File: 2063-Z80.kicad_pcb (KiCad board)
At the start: 4 copper layers, 100 x 100 mm, 80 parts, among them J1 Conn_01x05, J10 Conn_01x07, J11 Conn_02x03_Odd_Even, J2 DM3D-SF(41), J3 Conn_02x20_Counter_Clockwise, J4 Conn_02x05_Odd_Even, J5 Conn_02x05_Odd_Even, J6 0548190519, J7 Conn_02x13_Top_Bottom, J8 Conn_01x05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

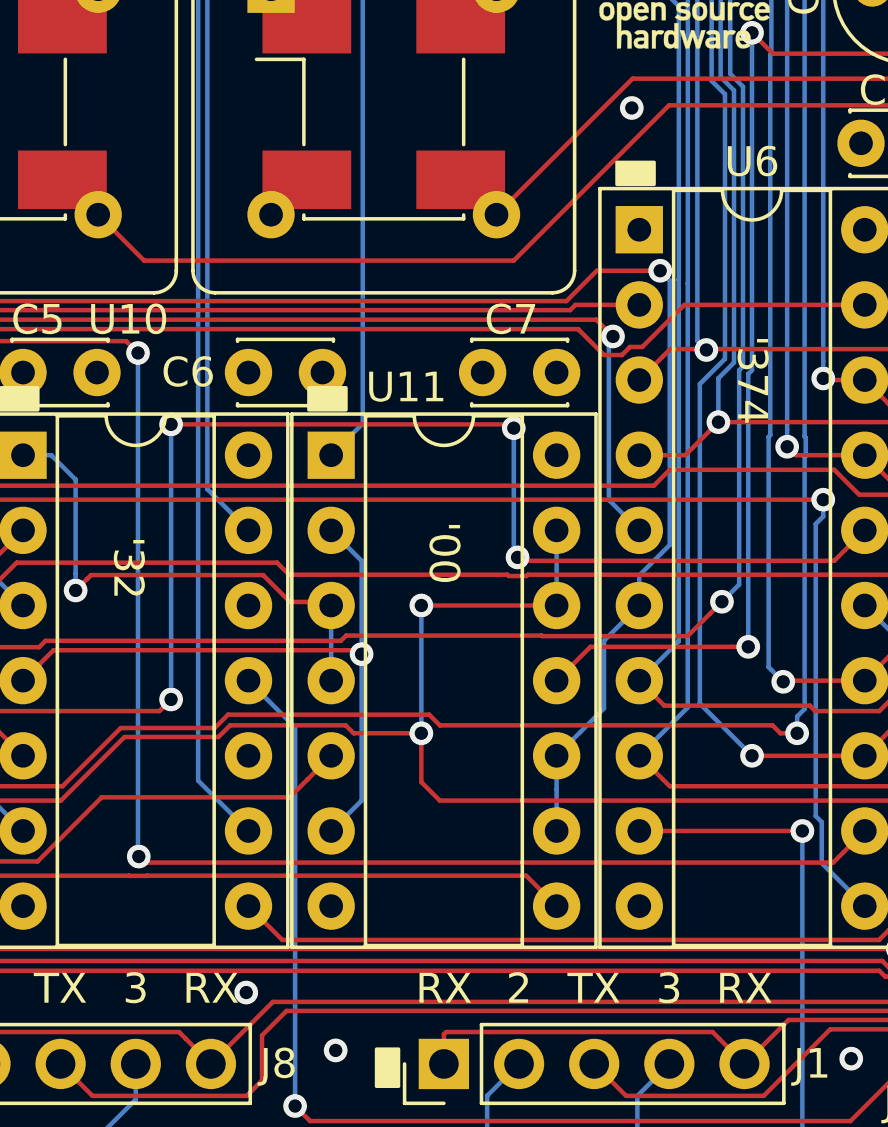
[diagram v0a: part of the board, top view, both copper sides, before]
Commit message: Change U11 symbol to a Schmitt NAND
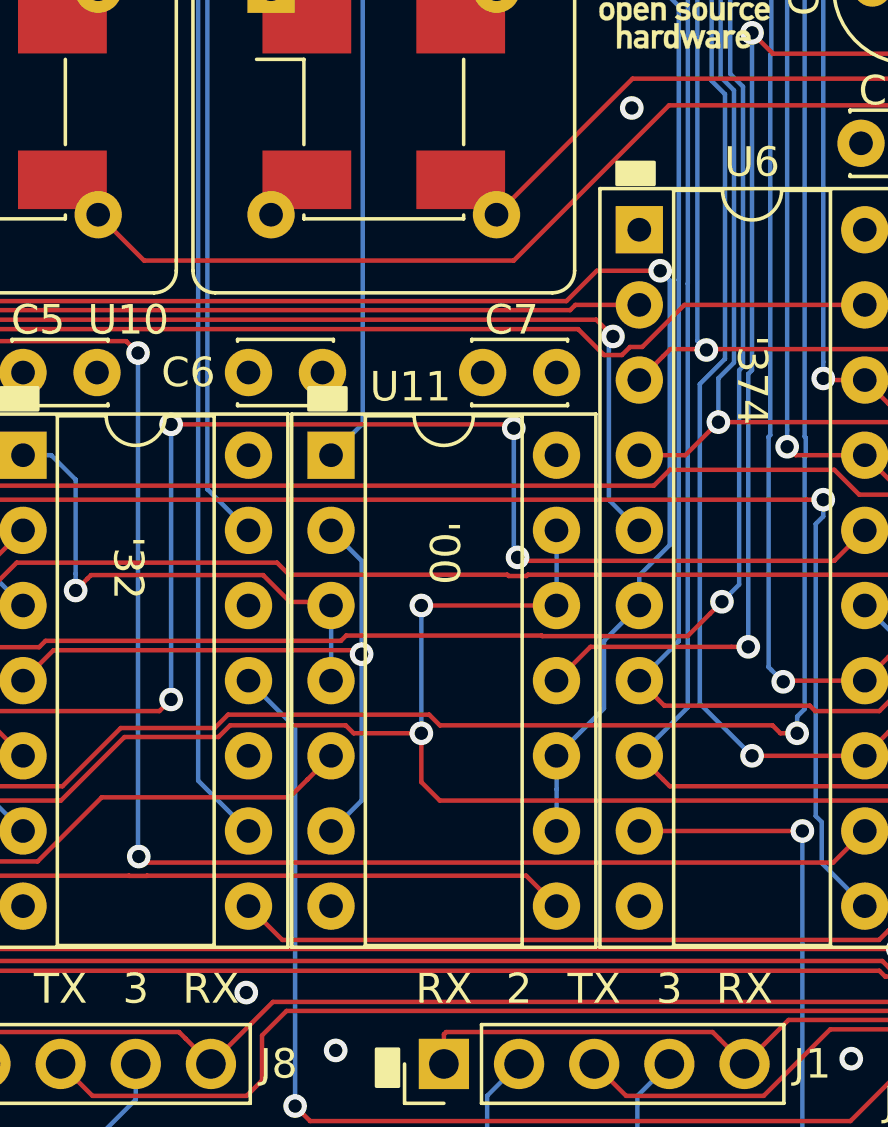
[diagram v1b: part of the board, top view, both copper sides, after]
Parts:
- U11: value 74HCT132E -> 74LS132
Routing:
- net /BAUD_CLK: track 65.6 -> 67.3 mm

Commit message: Revise BOM to reflect the as-built board.
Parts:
- U1: value Z80CPU -> Z80-CPU
- U10, U13: value 74LS32 -> 74HC32
- U11: value 74LS132 -> 74HCT132
- U4: value Z80_CTC -> Z80-CTC
- U6, U7: value 74LS374 -> 74HC374
- U9: value 74LS138 -> 74HC138
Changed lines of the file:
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@@
       (effects (font (size 1 1) (thickness 0.15)))
     )
-    (fp_text value 74LS132 (at 3.81 17.57) (layer F.Fab)
+    (fp_text value 74HCT132 (at 3.81 17.57) (layer F.Fab)
       (effects (font (size 1 1) (thickness 0.15)))
     )
@@
       (effects (font (size 1 1) (thickness 0.15)))
     )
-    (fp_text value 74LS32 (at 3.81 17.57) (layer F.Fab)
+    (fp_text value 74HC32 (at 3.81 17.57) (layer F.Fab)
       (effects (font (size 1 1) (thickness 0.15)))
     )
@@
       (effects (font (size 1 1) (thickness 0.15)))
     )
-    (fp_text value 74LS32 (at 3.81 17.57) (layer F.Fab)
+    (fp_text value 74HC32 (at 3.81 17.57) (layer F.Fab)
       (effects (font (size 1 1) (thickness 0.15)))
     )
@@
       (effects (font (size 1 1) (thickness 0.15)))
     )
-    (fp_text value Z80CPU (at 7.8994 45.5676) (layer F.Fab)
+    (fp_text value Z80-CPU (at 7.8994 45.5676) (layer F.Fab)
       (effects (font (size 1 1) (thickness 0.15)))
     )
@@
       (effects (font (size 1 1) (thickness 0.15)))
     )
-    (fp_text value Z80_CTC (at 7.62 35.35) (layer F.Fab)
+    (fp_text value Z80-CTC (at 7.62 35.35) (layer F.Fab)
       (effects (font (size 1 1) (thickness 0.15)))
     )
@@
       (effects (font (size 1 1) (thickness 0.15)))
     )
-    (fp_text value 74LS374 (at 3.81 25.19) (layer F.Fab)
+    (fp_text value 74HC374 (at 3.81 25.19) (layer F.Fab)
       (effects (font (size 1 1) (thickness 0.15)))
     )
@@
       (effects (font (size 1 1) (thickness 0.15)))
     )
-    (fp_text value 74LS374 (at 3.81 25.19) (layer F.Fab)
+    (fp_text value 74HC374 (at 3.81 25.19) (layer F.Fab)
       (effects (font (size 1 1) (thickness 0.15)))
     )
@@
       (effects (font (size 1 1) (thickness 0.15)))
     )
-    (fp_text value 74LS138 (at 3.81 20.11) (layer F.Fab)
+    (fp_text value 74HC138 (at 3.81 20.11) (layer F.Fab)
       (effects (font (size 1 1) (thickness 0.15)))
     )

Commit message: Clean up BOM values & formatting
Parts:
- J11: value Conn_02x03_Odd_Even -> Conn_02x03
- J3: value Conn_02x20_Counter_Clockwise -> Conn_02x20
- J4, J5: value Conn_02x05_Odd_Even -> Conn_02x05
- J7: value Conn_02x13_Top_Bottom -> Conn_02x13
- LOGO1, LOGO2: value Logo_Open_Hardware_Small -> OSHW_Logo
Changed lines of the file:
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@@
       (effects (font (size 1 1) (thickness 0.15)))
     )
-    (fp_text value Conn_02x03_Odd_Even (at 1.27 7.41 90) (layer F.Fab)
+    (fp_text value Conn_02x03 (at 1.27 7.41 90) (layer F.Fab)
       (effects (font (size 1 1) (thickness 0.15)))
     )
@@
       (effects (font (size 1 1) (thickness 0.15)))
     )
-    (fp_text value Conn_02x05_Odd_Even (at 1.27 12.49 90) (layer F.Fab)
+    (fp_text value Conn_02x05 (at 1.27 12.49 90) (layer F.Fab)
       (effects (font (size 1 1) (thickness 0.15)))
     )
@@
       (effects (font (size 1 1) (thickness 0.15)))
     )
-    (fp_text value Conn_02x05_Odd_Even (at 1.27 12.49 90) (layer F.Fab)
+    (fp_text value Conn_02x05 (at 1.27 12.49 90) (layer F.Fab)
       (effects (font (size 1 1) (thickness 0.15)))
     )
@@
       (effects (font (size 1 1) (thickness 0.15)))
     )
-    (fp_text value Logo_Open_Hardware_Small (at 0.75 0) (layer F.Fab) hide
+    (fp_text value OSHW_Logo (at 0.75 0) (layer F.Fab) hide
       (effects (font (size 1 1) (thickness 0.15)))
     )
@@
       (effects (font (size 1 1) (thickness 0.15)) (justify mirror))
     )
-    (fp_text value Logo_Open_Hardware_Small (at 0.75 0 90) (layer B.Fab) hide
+    (fp_text value OSHW_Logo (at 0.75 0 90) (layer B.Fab) hide
       (effects (font (size 1 1) (thickness 0.15)) (justify mirror))
     )
@@
       (effects (font (size 1 1) (thickness 0.15)))
     )
-    (fp_text value Conn_02x13_Top_Bottom (at 1.27 32.81 90) (layer F.Fab)
+    (fp_text value Conn_02x13 (at 1.27 32.81 90) (layer F.Fab)
       (effects (font (size 1 1) (thickness 0.15)))
     )
@@
       (effects (font (size 1 1) (thickness 0.15)))
     )
-    (fp_text value Conn_02x20_Counter_Clockwise (at 1.143 31.877 90) (layer F.Fab)
-      (effects (font (size 1 1) (thickness 0.15)))
-    )
+    (fp_text value Conn_02x20 (at 1.143 31.877 90) (layer F.Fab)
+      (effects (font (size 1 1) (thickness 0.15)))
+    )

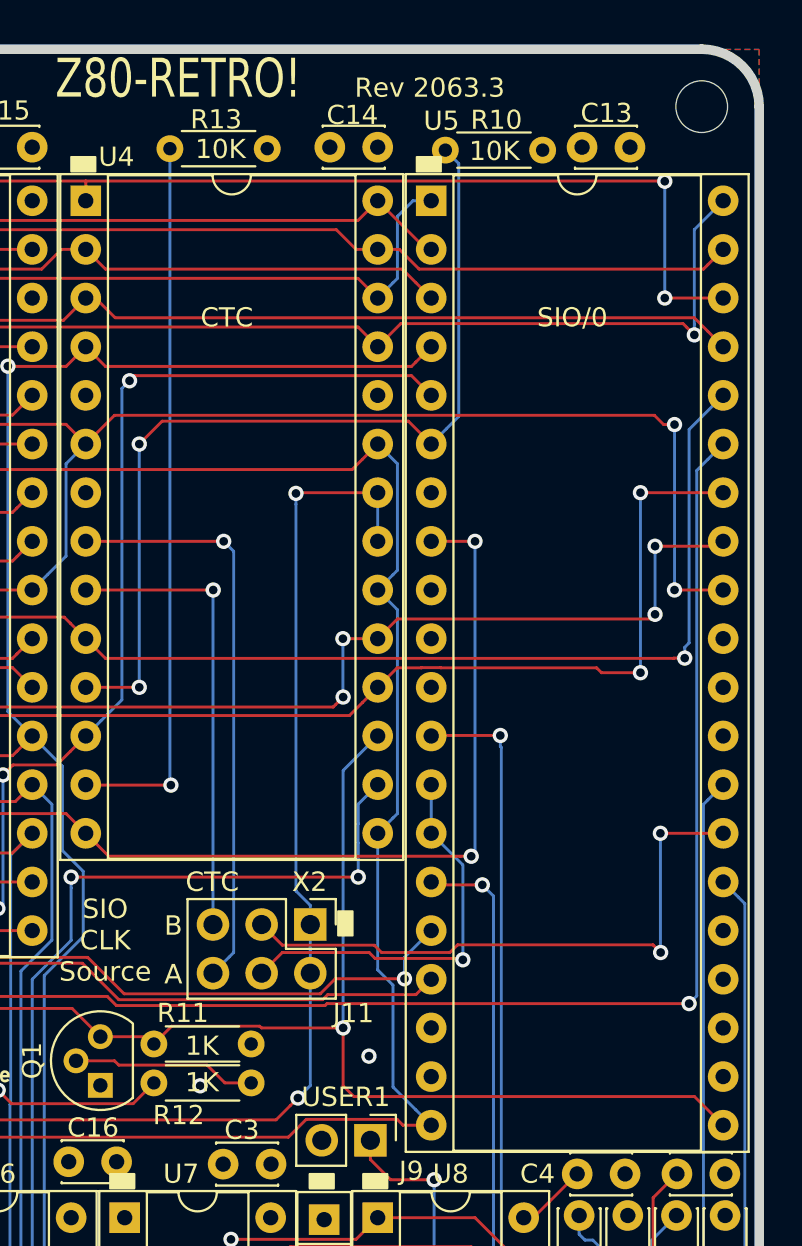
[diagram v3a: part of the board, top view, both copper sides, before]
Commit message: Move ~PRN_LF from U5.17 to U5.25
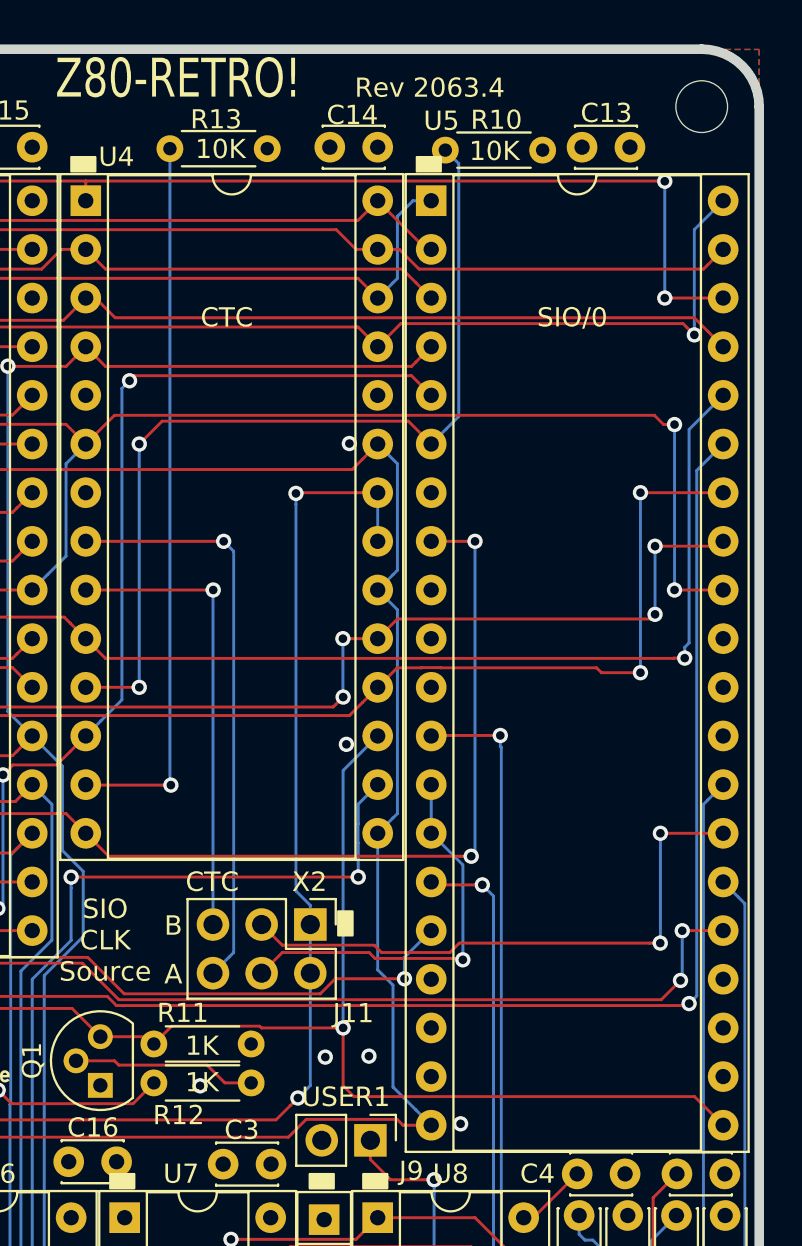
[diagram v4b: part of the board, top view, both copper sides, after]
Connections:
- U10 pad 13: /~RTSA -> /~DTRB
- U5 pad 17: /~RTSA -> Net-(U5-Pad17)
- U5 pad 25: Net-(U5-Pad25) -> /~DTRB
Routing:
- net /~DTRB: track 0.00 -> 83.0 mm, vias 0 -> 3
- net /~RTSA: track 65.2 -> 0.00 mm, vias 1 -> 0
- net /SIO_CLKB: track 31.3 -> 30.6 mm
- net GND: vias 16 -> 20
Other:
- board text added: "Rev 2063.4"
- board text removed: "Rev 2063.3"
